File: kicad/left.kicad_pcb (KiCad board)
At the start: 4 copper layers, 127.3 x 89.6 mm, 159 parts, among them M2 MountingHole_2.2mm_M2, Q1 PMF170XP,115, Q2 FS8205A_C2830320, SW1 TS-1088-AR02016, U1 TLV7031QDCKRQ1, U2 E73-2G4M08S1C, U3 SN74LVC1G74DQER, U4 BL8573CS8TR, U4 S2B-PH-K-S(LF)(SN), U7 LP5024RSMR, U8 DW01A_C42380662, X1 FC-13532.768KHZ9PF20PPM

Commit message: finished right, i hope
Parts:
- removed the U4 at (49.7, 43.6)
- removed U8: DW01A_C42380662, easyeda2kicad:SOT-23-6_L2.9-W1.6-P0.95-LS2.9-BL
- added U5: BL8573CS8TR, easyeda2kicad:ESOP-8_L4.9-W3.9-P1.27-LS6.0-BL-EP, B.Cu at (49.7, 43.6)
- added U6: DW01A_C42380662, easyeda2kicad:SOT-23-6_L2.9-W1.6-P0.95-LS2.9-BL, B.Cu at (44.7, 44.4)
- moved G*** 166.0 mm to (252.3, -6.80)
- moved G*** 166.0 mm to (262.7, 81.2)
- moved G** 101.4 mm to (142.5, -16.2)
- moved L1 0.68 mm to (45.5, 74.8)
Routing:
- net /VBUS: track 61.9 -> 74.8 mm, vias 4 -> 8
- net Net-(F1-Pad1): track 10.7 -> 21.0 mm, vias 2 -> 8
- net GND: track 119.3 -> 125.0 mm, vias 44 -> 47
- net /PWR: track 87.3 -> 92.5 mm, vias 24 -> 28
- net /STDBY: track 44.9 -> 46.2 mm
- net /BAT+: track 61.7 -> 62.8 mm
- net /VDD_nRF: track 53.1 -> 54.0 mm

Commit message: started left
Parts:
- removed S17: Choc HEX, hexcaps:PG1350_hotswap
- C1, C26, C27, C3, C4, C5, Fi4, Fi5, Fi6, L1, LED1, LED10, LED11, LED12, LED13, LED14, LED15, LED16, LED17, LED18, LED19, LED2, LED20, LED3, LED4, LED5, LED6, LED7, LED8, LED9, M2, R13, R14, R15, R16, R2, R3, R7, REF** (x2), SW1, U7, X1, hex_edge (x18): moved to B.Cu
- C10, C11, C12, C13, C14, C15, C16, C17, C18, C19, C20, C21, C22, C23, C24, C25, C6, C7, C8, C9, D10, D11, D12, D13, D14, D15, D16, D17, D18, D19, D2, D20, D3, D4, D5, D6, D7, D8, D9, Fi1, Fi2, Fi3, H1: moved to F.Cu
- S1, S10, S11, S12, S13, S14, S15, S16, S18, S19, S2, S20, S3, S4, S5, S6, S7, S8, S9: footprint hexcaps:PG1350_hotswap -> hexcaps:PG1350_hotswap_reversed; moved to F.Cu
- moved D2 128.8 mm to (24.4, 52.2), turned to 150 degrees
- moved D3 128.0 mm to (24.8, 72.6), turned to 150 degrees
- moved D4 128.0 mm to (24.8, 94.1), turned to 150 degrees
- moved Fi2 127.3 mm to (25.2, 49.0), turned to 0 degrees
- moved Fi1 126.7 mm to (152.2, 49.0), turned to 0 degrees
- moved Fi3 126.7 mm to (152.2, 113.4), turned to 0 degrees
- moved Fi4 126.7 mm to (152.2, 49.0), turned to 180 degrees
- moved Fi6 126.7 mm to (152.2, 113.4), turned to 180 degrees
- moved LED19 116.4 mm to (147.0, 109.4), turned to 150 degrees
- moved LED20 116.4 mm to (147.0, 44.9), turned to 150 degrees
- moved C6 113.7 mm to (31.9, 42.9), turned to 150 degrees
- moved C7 113.7 mm to (31.9, 64.4), turned to 150 degrees
- moved C8 113.7 mm to (31.9, 85.9), turned to 150 degrees
- moved Fi5 112.3 mm to (40.2, 49.0), turned to 180 degrees
- moved R2 111.9 mm to (144.8, 89.8), turned to 0 degrees
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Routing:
- net /COL2: track 253.5 -> 0.00 mm, vias 5 -> 0
- net /COL1: track 241.2 -> 0.00 mm, vias 3 -> 0
- net /ROW3: track 156.1 -> 334.0 mm, vias 5 -> 8
- net /COL3: track 207.4 -> 342.4 mm, vias 5 -> 10
- net /COL4: track 160.6 -> 39.1 mm, vias 3 -> 1
- net /LED1: track 110.6 -> 0.00 mm
- net /LED3: track 109.3 -> 0.00 mm
- net /LED2: track 98.9 -> 0.00 mm
- net /LED4: track 91.1 -> 0.00 mm
- net /LED6: track 86.4 -> 0.00 mm
- net /LED8: track 84.6 -> 0.00 mm
- net /CHRG: track 42.1 -> 122.2 mm, vias 1 -> 4
- net /LED5: track 75.9 -> 0.00 mm
- net /D+: track 72.2 -> 3.34 mm
- net /LED9: track 68.0 -> 0.00 mm
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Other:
- outline, holes or cut-outs redrawn

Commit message: moved  one mounting hole
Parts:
- moved Battery? 60.3 mm to (118.9, 75.3)
- moved REF** 16.0 mm to (152.9, 91.9)
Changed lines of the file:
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@@
 	(footprint "MountingHole:MountingHole_2.2mm_M2"
 		(layer "B.Cu")
-		(at 136.875082 91.9174 180)
+		(at 152.875082 91.9174 180)
 		(descr "Mounting Hole 2.2mm, M2, no annular, generated by kicad-footprint-generator mountinghole.py")
 		(tags "mountinghole M2")
@@
 	(footprint "my:3500mAh LiPo"
 		(layer "B.Cu")
-		(at 58.641066 75.287554 180)
+		(at 118.941066 75.287554 180)
 		(property "Reference" "Battery?"
 			(at 0 0.5 0)

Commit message: ...
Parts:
- added R17: RC0402FR-071ML, easyeda2kicad:R0402, F.Cu at (138.2, 72.8)
- added R18: WR04W2494FTL, easyeda2kicad:R0402, F.Cu at (140.3, 72.8)
- added S17: Choc HEX, hexcaps:PG1350_hotswap_reversed, F.Cu at (107.4, 70.4)
- C1, C26, C27, C3, C4, C5, L1, LED1, LED10, LED11, LED12, LED13, LED14, LED15, LED16, LED17, LED18, LED19, LED2, LED20, LED3, LED4, LED5, LED6, LED7, LED8, LED9, R13, R14, R15, R16, R2, R3, R7, SW1, U7, X1: moved to F.Cu
- C10, C11, C12, C13, C14, C15, C16, C17, C18, C19, C20, C21, C22, C23, C24, C25, C6, C7, C8, C9, D10, D11, D12, D13, D14, D15, D16, D17, D18, D19, D2, D20, D3, D4, D5, D6, D7, D8, D9, H1: moved to B.Cu
- moved R7 30.5 mm to (137.3, 96.2)
- moved C4 30.5 mm to (139.2, 96.1)
- moved SW1 26.0 mm to (138.1, 93.9)
- moved C5 18.6 mm to (136.9, 90.4), turned to -90 degrees
- moved R2 16.9 mm to (144.6, 72.8)
- moved R3 16.9 mm to (142.4, 72.8)
- moved Fi2 15.0 mm to (40.2, 49.0)
- moved L1 12.9 mm to (131.3, 87.7)
- moved D8 12.0 mm to (91.0, 110.8), turned to -30 degrees
- moved D10 12.0 mm to (72.5, 57.0), turned to -30 degrees
- moved D5 12.0 mm to (54.0, 46.3), turned to -30 degrees
- moved D9 12.0 mm to (72.5, 35.5), turned to -30 degrees
- moved D11 12.0 mm to (72.5, 78.5), turned to -30 degrees
- moved D2 12.0 mm to (34.9, 58.2), turned to -30 degrees
- moved D3 12.0 mm to (35.3, 78.5), turned to -30 degrees
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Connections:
- U2 pad 1: /COL7 -> /STDBY
- U2 pad 12: /ROW3 -> unconnected-(U2-P0.26-Pad12)
- U2 pad 15: unconnected-(U2-AI3-Pad15) -> /LED_EN
- U2 pad 16: unconnected-(U2-P0.08-Pad16) -> /LED_SDA
- U2 pad 17: /COL6 -> /LED_SCL
- U2 pad 2: unconnected-(U2-P1.10-Pad2) -> /CHRG
- U2 pad 28: /ROW1 -> unconnected-(U2-P15-Pad28)
- U2 pad 3: unconnected-(U2-P0.03-Pad3) -> /PWR_BTN_PRESS
- U2 pad 32: /COL4 -> /COL1
- U2 pad 33: unconnected-(U2-P0.13-Pad33) -> /ROW3
- U2 pad 34: /COL3 -> /COL2
- U2 pad 36: /COL2 -> /COL3
- U2 pad 37: /SWDIO -> /SWBCLK
- U2 pad 38: /COL1 -> /COL4
- U2 pad 39: /SWBCLK -> /SWDIO
- U2 pad 40: unconnected-(U2-P1.04-Pad40) -> /COL5
- U2 pad 41: /STDBY -> unconnected-(U2-NF1-Pad41)
- U2 pad 42: unconnected-(U2-P1.06-Pad42) -> /ROW4
- U2 pad 43: /CHRG -> unconnected-(U2-NF2-Pad43)
- U2 pad 6: /COL5 -> unconnected-(U2-P1.13-Pad6)
- U2 pad 7: /LED_EN -> unconnected-(U2-AI0-Pad7)
- U2 pad 8: /LED_SDA -> unconnected-(U2-AI5-Pad8)
- U2 pad 9: /LED_SCL -> /ROW1
- U7 pad 1: /LED19 -> /LED20
- U7 pad 10: /LED3 -> /LED17
- U7 pad 11: /LED2 -> /LED13
- U7 pad 12: /LED5 -> /LED9
- U7 pad 13: /LED9 -> /LED5
- U7 pad 14: /LED13 -> /LED2
- U7 pad 15: /LED17 -> /LED3
- U7 pad 17: /LED1 -> /LED6
- U7 pad 18: /LED4 -> /LED10
- U7 pad 19: /LED8 -> /LED14
- U7 pad 2: /LED15 -> unconnected-(U7-OUT1-Pad2)
- U7 pad 20: /LED12 -> /LED18
- U7 pad 21: /LED16 -> /LED7
- U7 pad 22: unconnected-(U7-OUT21-Pad22) -> /LED11
- U7 pad 23: unconnected-(U7-OUT22-Pad23) -> /LED15
- U7 pad 24: /LED20 -> /LED19
- U7 pad 3: /LED11 -> unconnected-(U7-OUT2-Pad3)
- U7 pad 4: /LED7 -> /LED16
- U7 pad 5: /LED18 -> /LED12
- U7 pad 6: /LED14 -> /LED8
- U7 pad 7: /LED10 -> /LED4
- U7 pad 8: /LED6 -> /LED1
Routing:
- net /COL3: track 342.4 -> 106.2 mm, vias 10 -> 1
- net /ROW2: track 234.1 -> 0.00 mm, vias 1 -> 0
- net /ROW3: track 334.0 -> 134.7 mm, vias 8 -> 3
- net /ROW1: track 138.5 -> 0.00 mm, vias 1 -> 0
- net /COL2: track 0.00 -> 111.3 mm, vias 0 -> 1
- net /CHRG: track 122.2 -> 38.1 mm, vias 4 -> 3
- net /COL5: track 66.3 -> 130.1 mm, vias 2 -> 1
- net /COL1: track 0.00 -> 56.4 mm, vias 0 -> 1
- net /PWR: track 63.6 -> 119.5 mm
- net /COL4: track 39.1 -> 92.6 mm
- net /ROW4: track 76.2 -> 109.7 mm, vias 0 -> 1
- net /STDBY: track 3.11 -> 34.7 mm, vias 1 -> 3
- net GND: track 118.2 -> 96.7 mm, vias 47 -> 52
- net /SWDIO: track 31.9 -> 11.5 mm, vias 1 -> 0
- net /SWBCLK: track 31.3 -> 11.3 mm, vias 1 -> 0
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
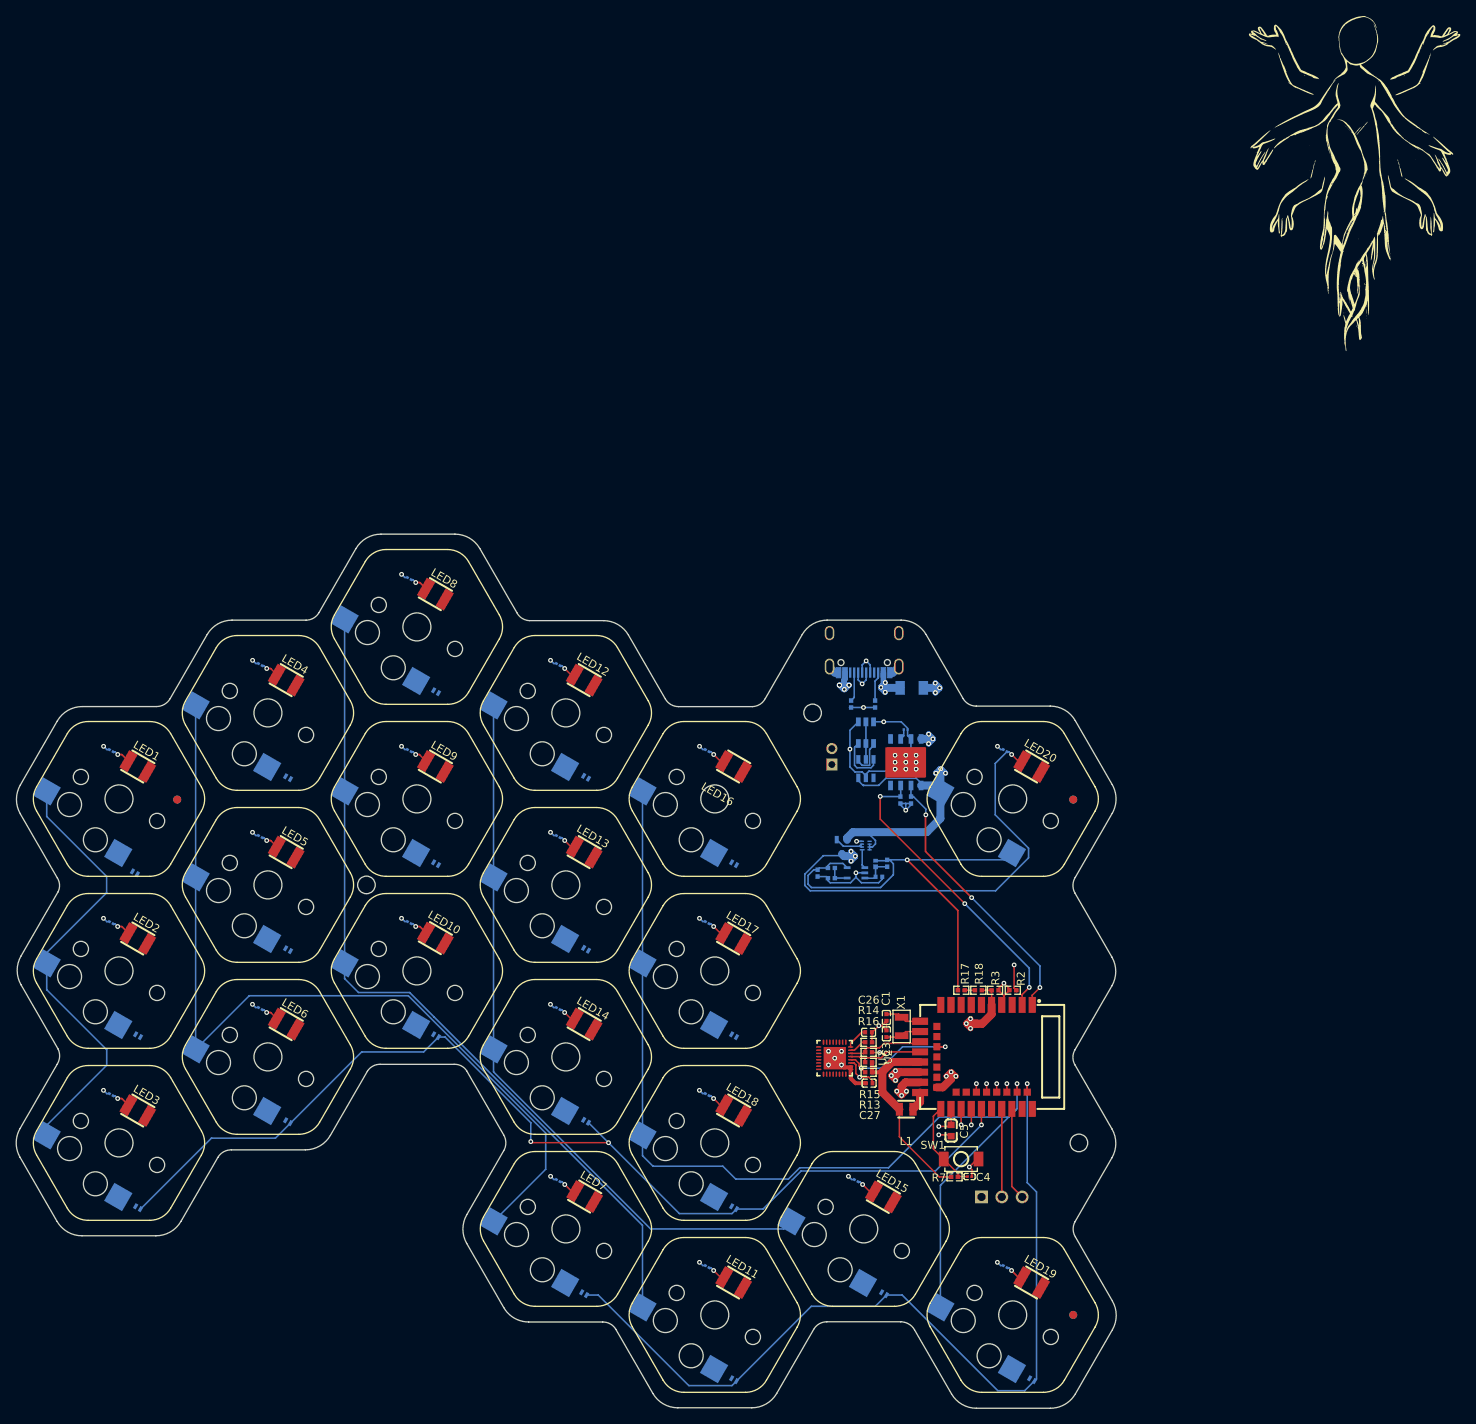
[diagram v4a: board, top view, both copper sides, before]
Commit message: left wiring done... right changed to shmitt inctead of comparator... need to do same on left... fixing of right in progress
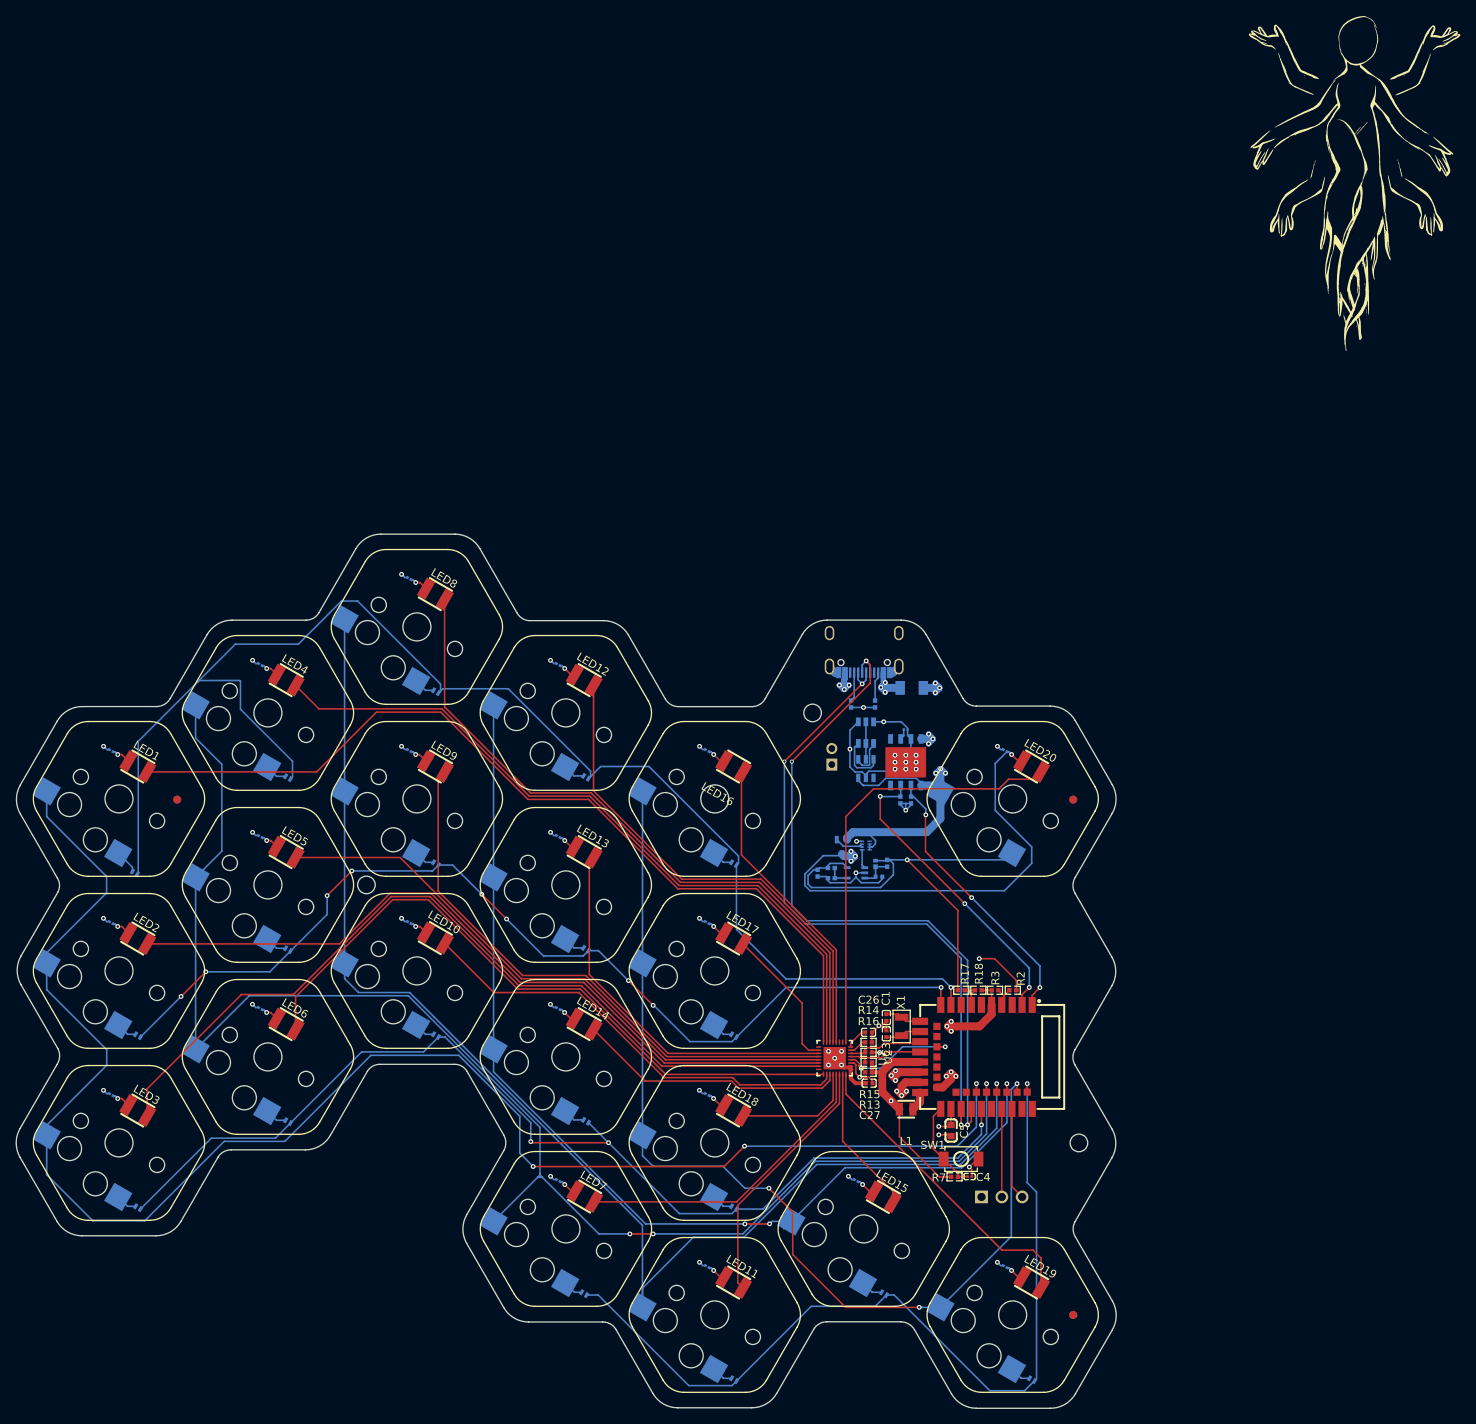
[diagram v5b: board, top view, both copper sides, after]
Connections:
- U2 pad 3: /PWR_BTN_PRESS -> unconnected-(U2-P0.03-Pad3)
- U2 pad 7: unconnected-(U2-AI0-Pad7) -> /PWR_BTN_PRESS
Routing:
- net /ROW1: track 0.00 -> 177.6 mm, vias 0 -> 1
- net /COL1: track 56.4 -> 204.4 mm, vias 1 -> 3
- net /ROW2: track 0.00 -> 125.1 mm, vias 0 -> 9
- net /LED1: track 0.00 -> 111.1 mm
- net /LED3: track 0.00 -> 106.1 mm
- net /LED2: track 0.00 -> 95.4 mm
- net /LED4: track 0.00 -> 91.3 mm
- net /LED8: track 0.00 -> 85.5 mm
- net /LED6: track 0.00 -> 84.2 mm
- net /D+: track 5.34 -> 85.9 mm, vias 2 -> 3
- net /D-: track 5.23 -> 82.4 mm, vias 2 -> 3
- net /LED5: track 0.00 -> 75.9 mm
- net /COL2: track 111.3 -> 184.9 mm, vias 1 -> 3
- net /LED9: track 0.00 -> 71.4 mm
- net /LED12: track 0.00 -> 62.8 mm
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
